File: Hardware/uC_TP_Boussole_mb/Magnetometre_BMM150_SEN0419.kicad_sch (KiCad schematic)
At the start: 2 parts, among them J5 Conn_01x09

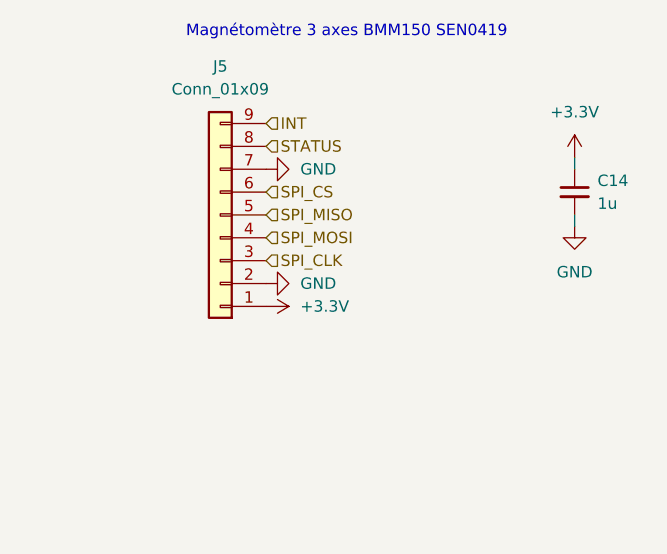
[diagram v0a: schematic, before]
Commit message: starting pin out nucleo
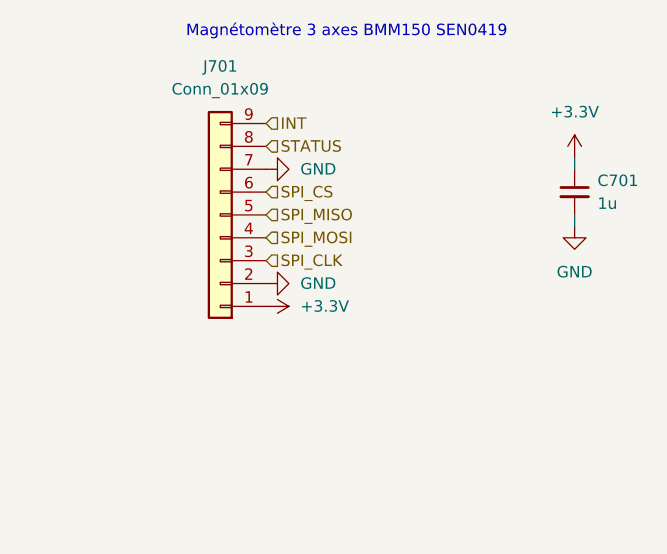
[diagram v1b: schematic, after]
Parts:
- C701: renamed from C14; footprint (none) -> Capacitor_SMD:C_0402_1005Metric
- J701: renamed from J5; footprint (none) -> Connector_JST:JST_XH_S9B-XH-A_1x09_P2.50mm_Horizontal
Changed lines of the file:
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@@
 		(dnp no)
 		(fields_autoplaced yes)
-		(property "Reference" "#PWR046"
+		(property "Reference" "#PWR0705"
 			(at 69.85 55.88 0)
 			(effects
@@
 			(project "uC_TP_Boussole_mb"
 				(path "/2e9feef3-d2ce-488a-99fa-e1de5099ffc3/aacdf244-528b-4ec8-923e-bfdb7275b7de"
-					(reference "#PWR046")
+					(reference "#PWR0705")
 					(unit 1)
 				)
@@
 		(dnp no)
 		(fields_autoplaced yes)
-		(property "Reference" "#PWR042"
+		(property "Reference" "#PWR0701"
 			(at 41.91 43.18 0)
 			(effects
@@
 			(project "uC_TP_Boussole_mb"
 				(path "/2e9feef3-d2ce-488a-99fa-e1de5099ffc3/aacdf244-528b-4ec8-923e-bfdb7275b7de"
-					(reference "#PWR042")
+					(reference "#PWR0701")
 					(unit 1)
 				)
@@
 		(dnp no)
 		(fields_autoplaced yes)
-		(property "Reference" "C14"
+		(property "Reference" "C701"
 			(at 72.39 44.4562 0)
 			(effects
@@
 			)
 		)
-		(property "Footprint" ""
+		(property "Footprint" "Capacitor_SMD:C_0402_1005Metric"
 			(at 69.85 45.72 0)
 			(effects
@@
 			(project "uC_TP_Boussole_mb"
 				(path "/2e9feef3-d2ce-488a-99fa-e1de5099ffc3/aacdf244-528b-4ec8-923e-bfdb7275b7de"
-					(reference "C14")
+					(reference "C701")
 					(unit 1)
 				)
@@
 		(dnp no)
 		(fields_autoplaced yes)
-		(property "Reference" "#PWR045"
+		(property "Reference" "#PWR0704"
 			(at 69.85 45.72 0)
 			(effects
@@
 			(project "uC_TP_Boussole_mb"
 				(path "/2e9feef3-d2ce-488a-99fa-e1de5099ffc3/aacdf244-528b-4ec8-923e-bfdb7275b7de"
-					(reference "#PWR045")
+					(reference "#PWR0704")
 					(unit 1)
 				)
@@
 		(dnp no)
 		(fields_autoplaced yes)
-		(property "Reference" "#PWR044"
+		(property "Reference" "#PWR0703"
 			(at 31.75 58.42 0)
 			(effects
@@
 			(project "uC_TP_Boussole_mb"
 				(path "/2e9feef3-d2ce-488a-99fa-e1de5099ffc3/aacdf244-528b-4ec8-923e-bfdb7275b7de"
-					(reference "#PWR044")
+					(reference "#PWR0703")
 					(unit 1)
 				)
@@
 		(dnp no)
 		(fields_autoplaced yes)
-		(property "Reference" "J5"
+		(property "Reference" "J701"
 			(at 30.48 31.75 0)
 			(effects
@@
 			)
 		)
-		(property "Footprint" ""
+		(property "Footprint" "Connector_JST:JST_XH_S9B-XH-A_1x09_P2.50mm_Horizontal"
 			(at 30.48 48.26 0)
 			(effects
@@
 			(project "uC_TP_Boussole_mb"
 				(path "/2e9feef3-d2ce-488a-99fa-e1de5099ffc3/aacdf244-528b-4ec8-923e-bfdb7275b7de"
-					(reference "J5")
+					(reference "J701")
 					(unit 1)
 				)
@@
 		(dnp no)
 		(fields_autoplaced yes)
-		(property "Reference" "#PWR043"
+		(property "Reference" "#PWR0702"
 			(at 41.91 55.88 0)
 			(effects
@@
 			(project "uC_TP_Boussole_mb"
 				(path "/2e9feef3-d2ce-488a-99fa-e1de5099ffc3/aacdf244-528b-4ec8-923e-bfdb7275b7de"
-					(reference "#PWR043")
-					(unit 1)
-				)
+					(reference "#PWR0702")
+					(unit 1)
+				)

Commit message: update schematic
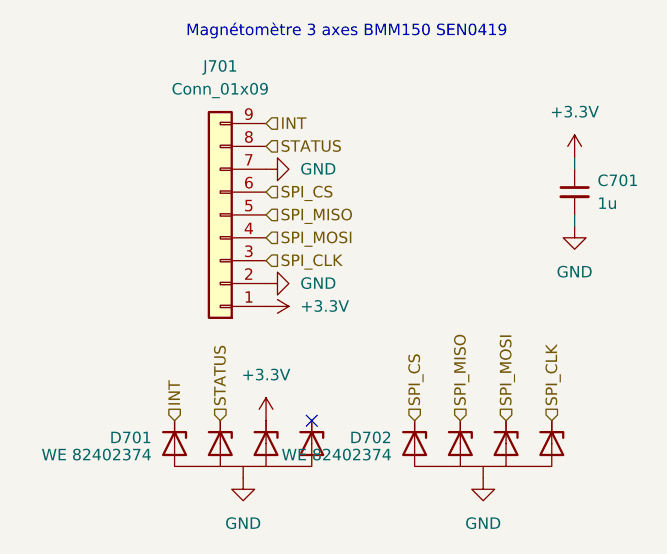
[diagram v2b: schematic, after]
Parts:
- added D701, D702: WE 82402374, libs:SC70-5L, symbol mylibs:D_TVS_Uni_x4
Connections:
- net +3.3V: now also D701.3 (I/O)
- net GND: now also D701.2 (GND), D702.2 (GND)
- net INT: now also D701.5 (I/O)
- net SPI_CLK: now also D702.1 (I/O)
- net SPI_CS: now also D702.5 (I/O)
- net SPI_MISO: now also D702.4 (I/O)
- net SPI_MOSI: now also D702.3 (I/O)
- net STATUS: now also D701.4 (I/O)
- no-connect marks 0 -> 1

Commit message: finalize pcb
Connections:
- net INT: now also D702.5 (I/O); no longer D701.5 (I/O)
- net SPI_CLK: now also D701.4 (I/O); no longer D702.1 (I/O)
- net SPI_CS: now also D702.3 (I/O); no longer D702.5 (I/O)
- net SPI_MISO: now also D702.1 (I/O); no longer D702.4 (I/O)
- net SPI_MOSI: now also D701.5 (I/O); no longer D702.3 (I/O)
- net STATUS: now also D702.4 (I/O); no longer D701.4 (I/O)
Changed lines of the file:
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@@
 		)
 	)
-	(hierarchical_label "SPI_MOSI"
+	(hierarchical_label "STATUS"
 		(shape input)
-		(at 62.23 71.12 90)
+		(at 57.15 71.12 90)
 		(fields_autoplaced yes)
 		(effects
@@
 		(shape input)
 		(at 35.56 53.34 0)
+		(fields_autoplaced yes)
+		(effects
+			(font
+				(size 1.27 1.27)
+			)
+			(justify left)
+		)
+	)
+	(hierarchical_label "INT"
+		(shape input)
+		(at 52.07 71.12 90)
+		(fields_autoplaced yes)
+		(effects
+			(font
+				(size 1.27 1.27)
+			)
+			(justify left)
+		)
+	)
+	(hierarchical_label "SPI_CLK"
+		(shape input)
+		(at 30.48 71.12 90)
 		(fields_autoplaced yes)
 		(effects
@@
 	(hierarchical_label "SPI_MISO"
 		(shape input)
-		(at 35.56 48.26 0)
+		(at 67.31 71.12 90)
 		(fields_autoplaced yes)
 		(effects
@@
 		)
 	)
-	(hierarchical_label "INT"
+	(hierarchical_label "SPI_MISO"
 		(shape input)
-		(at 25.4 71.12 90)
+		(at 35.56 48.26 0)
 		(fields_autoplaced yes)
 		(effects
@@
 	(hierarchical_label "SPI_CS"
 		(shape input)
-		(at 35.56 45.72 0)
-		(fields_autoplaced yes)
-		(effects
-			(font
-				(size 1.27 1.27)
-			)
-			(justify left)
-		)
-	)
-	(hierarchical_label "SPI_MISO"
-		(shape input)
-		(at 57.15 71.12 90)
-		(fields_autoplaced yes)
-		(effects
-			(font
-				(size 1.27 1.27)
-			)
-			(justify left)
-		)
-	)
-	(hierarchical_label "STATUS"
-		(shape input)
-		(at 30.48 71.12 90)
-		(fields_autoplaced yes)
-		(effects
-			(font
-				(size 1.27 1.27)
-			)
-			(justify left)
-		)
-	)
-	(hierarchical_label "SPI_CLK"
-		(shape input)
-		(at 67.31 71.12 90)
+		(at 62.23 71.12 90)
 		(fields_autoplaced yes)
 		(effects
@@
 	(hierarchical_label "SPI_CS"
 		(shape input)
-		(at 52.07 71.12 90)
+		(at 35.56 45.72 0)
 		(fields_autoplaced yes)
 		(effects
+			(font
+				(size 1.27 1.27)
+			)
+			(justify left)
+		)
+	)
+	(hierarchical_label "SPI_MOSI"
+		(shape input)
+		(at 25.4 71.12 90)
+		(fields_autoplaced yes)
+		(effects

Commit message: bom
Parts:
- J701: MPN (none) -> S9B-XH-A (LF)(SN)
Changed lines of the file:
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@@
+			)
+		)
+		(property "MPN" "S9B-XH-A (LF)(SN)"
+			(at 30.48 48.26 0)
+			(effects
+				(font
+					(size 1.27 1.27)
+				)
+				(hide yes)
 			)
 		)
